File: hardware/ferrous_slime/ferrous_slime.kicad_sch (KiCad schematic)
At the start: 53 parts, among them J1 IMU_Connector, J2 Battery_Connector, J3 USB_C_Receptacle_USB2.0, J4 Unused_IO, Q1 DMG3415U, SW1 SW_PWR, U1 BNO/MPU/ICM_Break, U2 ESP32-C3-MINI-1, U3 TP4056, U4 M3406, Y1 32.768Hz

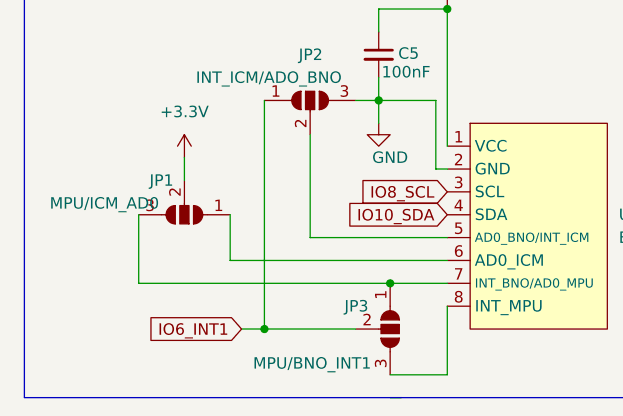
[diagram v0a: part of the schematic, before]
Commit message: Fixed jumper silkscreens and added double ground plane
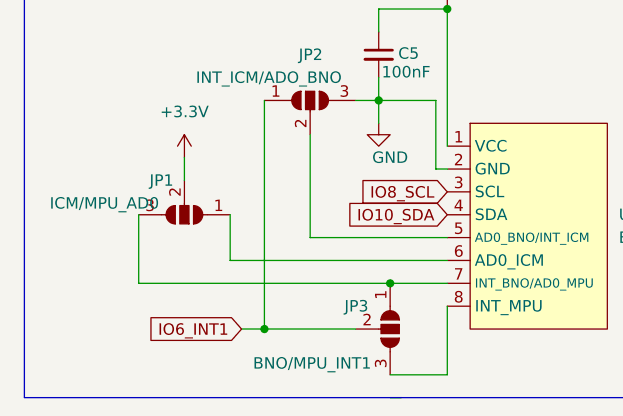
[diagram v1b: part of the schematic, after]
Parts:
- JP1: value MPU/ICM_AD0 -> ICM/MPU_AD0
- JP3: value MPU/BNO_INT1 -> BNO/MPU_INT1
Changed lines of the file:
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@@
       (effects (font (size 1.27 1.27)) (justify left))
     )
-    (property "Value" "MPU/BNO_INT1" (id 1) (at 39.37 161.29 90)
+    (property "Value" "BNO/MPU_INT1" (id 1) (at 39.37 161.29 90)
       (effects (font (size 1.27 1.27)) (justify left))
     )
@@
     (in_bom yes) (on_board yes)
     (property "Reference" "JP1" (id 0) (at 29.21 140.97 0))
-    (property "Value" "MPU/ICM_AD0" (id 1) (at 22.86 143.51 0))
+    (property "Value" "ICM/MPU_AD0" (id 1) (at 22.86 143.51 0))
     (property "Footprint" "Jumper:SolderJumper-3_P1.3mm_Open_Pad1.0x1.5mm" (id 2) (at 31.75 144.78 0)
       (effects (font (size 1.27 1.27)) hide)
@@
     )
     (path "/c4529189-45d4-4fb2-a639-86f5fb6b04c1"
-      (reference "JP1") (unit 1) (value "MPU/ICM_AD0") (footprint "Jumper:SolderJumper-3_P1.3mm_Open_Pad1.0x1.5mm")
+      (reference "JP1") (unit 1) (value "ICM/MPU_AD0") (footprint "Jumper:SolderJumper-3_P1.3mm_Open_Pad1.0x1.5mm")
     )
     (path "/3376fce4-7c2a-4830-8668-5c55f20711b2"
@@
     )
     (path "/9b1a0ddc-2815-4f35-824b-9e81fbeabbd5"
-      (reference "JP3") (unit 1) (value "MPU/BNO_INT1") (footprint "Jumper:SolderJumper-3_P1.3mm_Open_Pad1.0x1.5mm")
+      (reference "JP3") (unit 1) (value "BNO/MPU_INT1") (footprint "Jumper:SolderJumper-3_P1.3mm_Open_Pad1.0x1.5mm")
     )
     (path "/32aeb981-ffe8-4bff-a65d-ee3788161f8a"

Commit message: Annotated pins and added silkscreen art
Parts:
- J4: footprint Connector_PinHeader_2.54mm:PinHeader_1x07_P2.54mm_Vertical -> slimevr_pcb:IO_Breakouts
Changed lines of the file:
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@@
       (effects (font (size 1.27 1.27)) (justify left))
     )
-    (property "Footprint" "Connector_PinHeader_2.54mm:PinHeader_1x07_P2.54mm_Vertical" (id 2) (at 147.32 153.67 0)
+    (property "Footprint" "slimevr_pcb:IO_Breakouts" (id 2) (at 147.32 153.67 0)
       (effects (font (size 1.27 1.27)) hide)
     )
@@
     )
     (path "/07ba3b11-b85a-4d64-9bdc-e0f731b1e86f"
-      (reference "J4") (unit 1) (value "Unused_IO") (footprint "Connector_PinHeader_2.54mm:PinHeader_1x07_P2.54mm_Vertical")
+      (reference "J4") (unit 1) (value "Unused_IO") (footprint "slimevr_pcb:IO_Breakouts")
     )
     (path "/c4529189-45d4-4fb2-a639-86f5fb6b04c1"

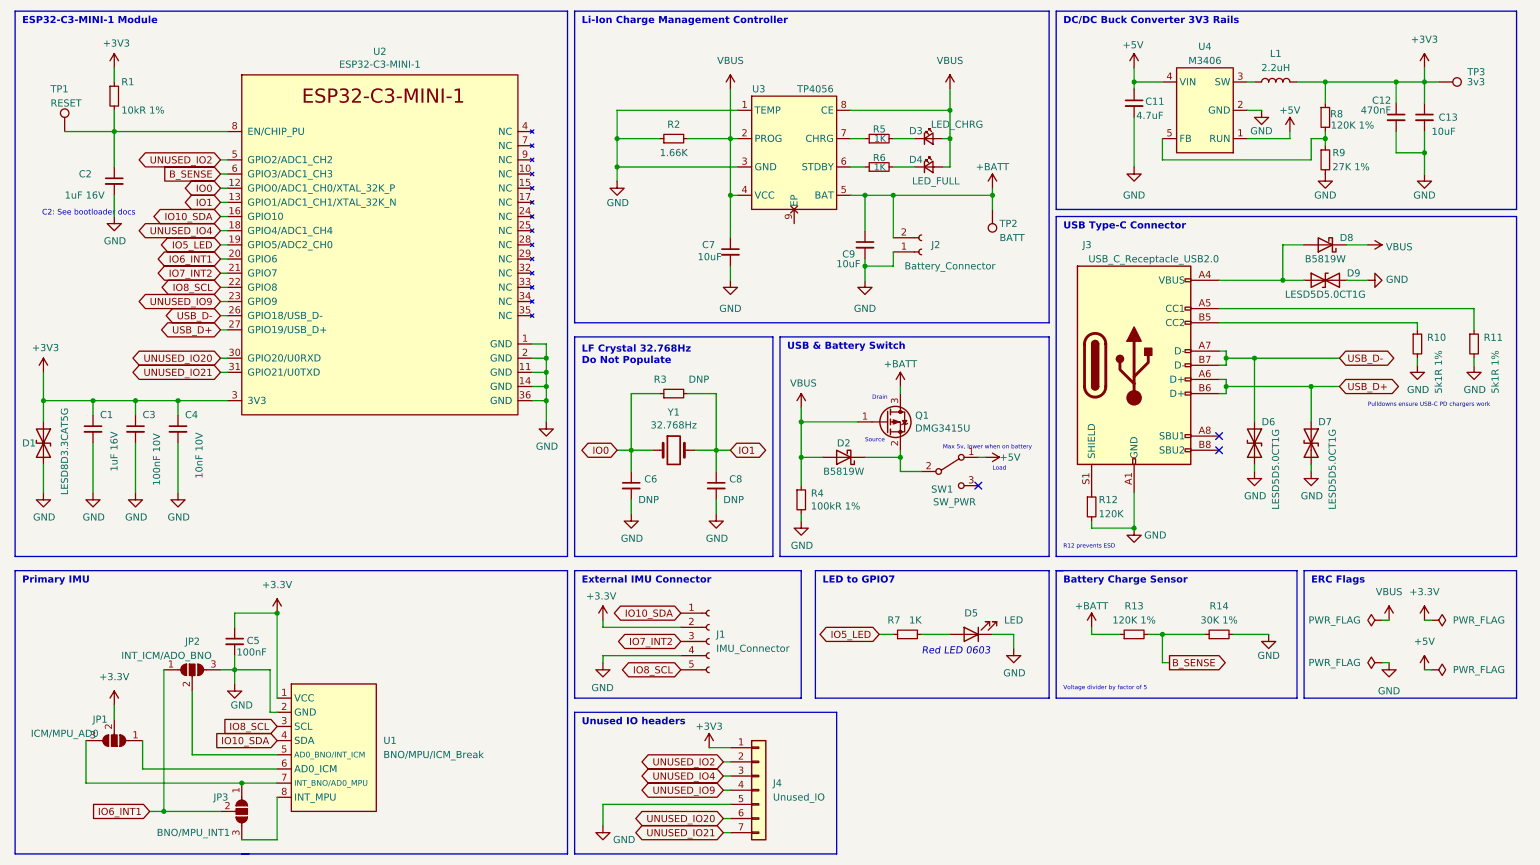
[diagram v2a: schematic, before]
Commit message: Removed Rust_Board and updated all renders/plots
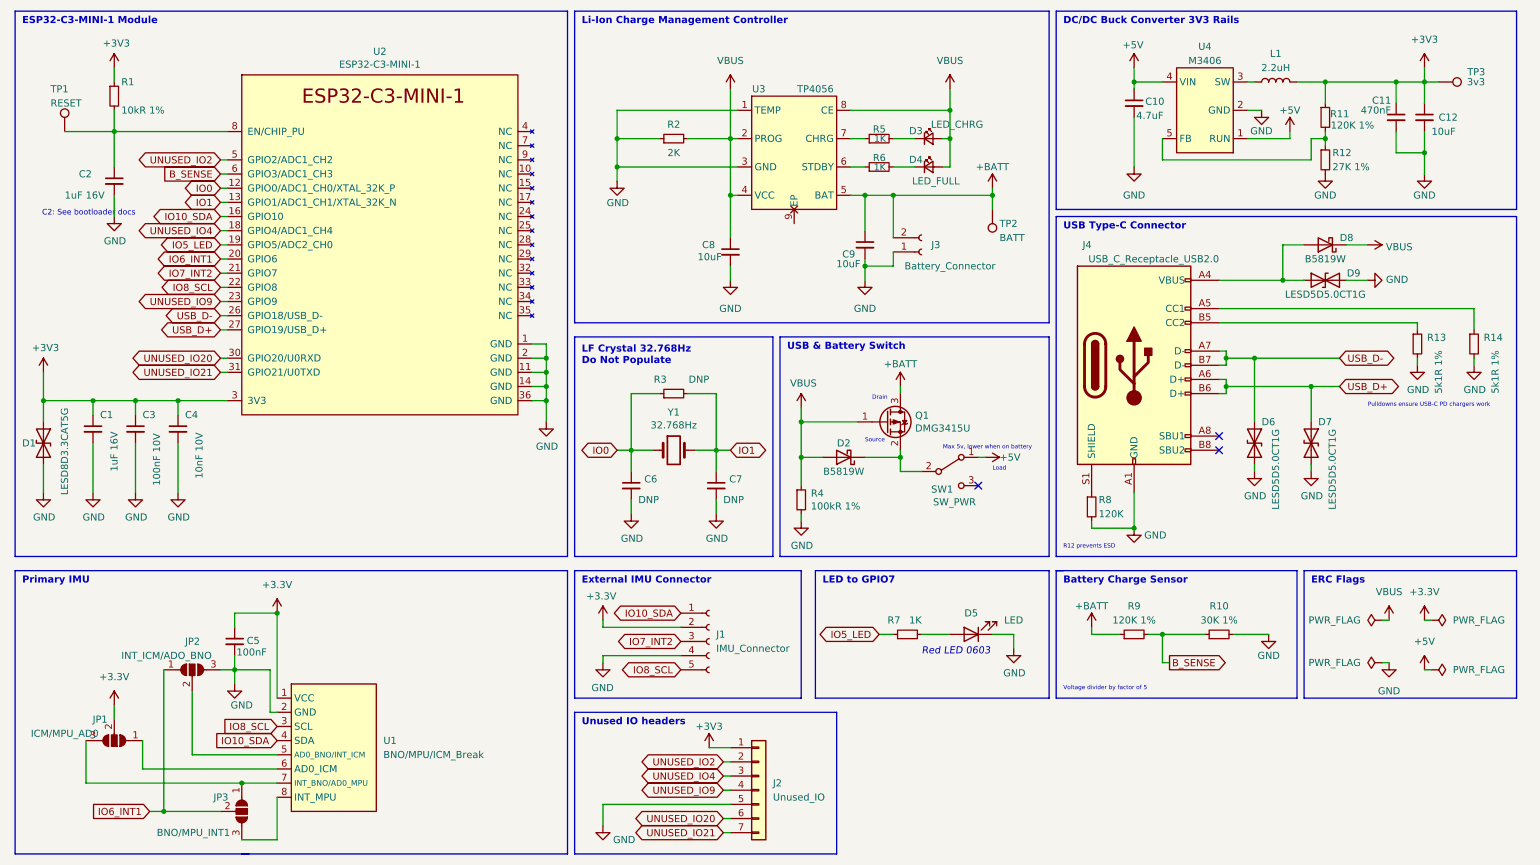
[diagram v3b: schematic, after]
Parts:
- R2: value 1.66K -> 2K
- renumbered C11 to C10, C12 to C11, C13 to C12, C8 to C7, C7 to C8, J4 to J2, J2 to J3, J3 to J4, R14 to R10, R8 to R11, R9 to R12, R10 to R13, R11 to R14, R12 to R8, R13 to R9

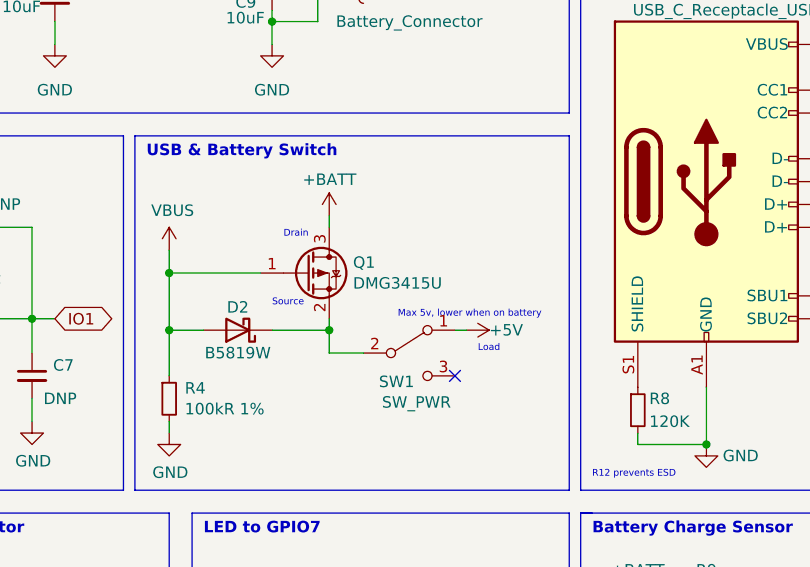
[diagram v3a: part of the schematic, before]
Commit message: Added refs to silkscreen
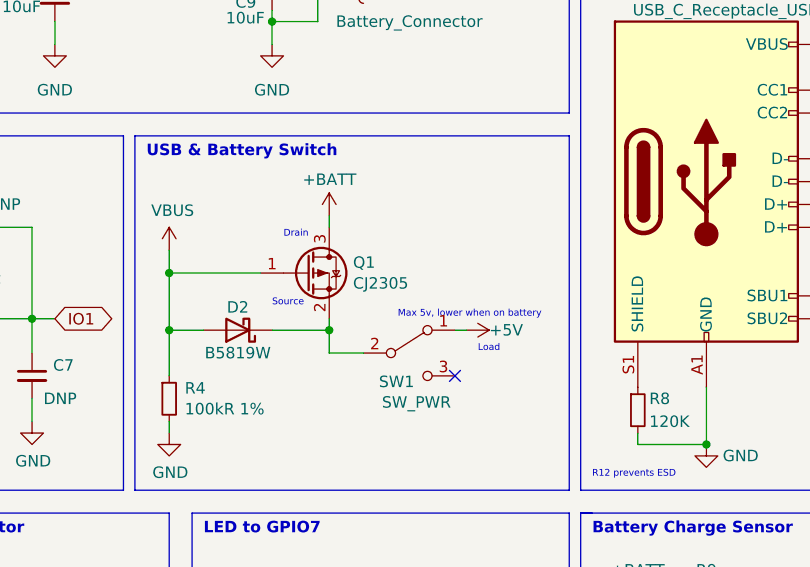
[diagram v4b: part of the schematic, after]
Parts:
- Q1: value DMG3415U -> CJ2305
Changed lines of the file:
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@@
       (effects (font (size 1.27 1.27)) (justify left))
     )
-    (property "Value" "DMG3415U" (id 1) (at 175.3616 88.773 0)
+    (property "Value" "CJ2305" (id 1) (at 175.3616 88.773 0)
       (effects (font (size 1.27 1.27)) (justify left))
     )
@@
     )
     (path "/00000000-0000-0000-0000-0000628bb66a"
-      (reference "Q1") (unit 1) (value "DMG3415U") (footprint "Package_TO_SOT_SMD:SOT-23")
+      (reference "Q1") (unit 1) (value "CJ2305") (footprint "Package_TO_SOT_SMD:SOT-23")
     )
     (path "/00000000-0000-0000-0000-000061cdb32a"

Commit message: v0.1.0 board released
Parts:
- D1: footprint Diode_SMD:D_SOD-323_HandSoldering -> slimevr_pcb:SOD882
- L1: footprint Inductor_SMD:L_7.3x7.3_H4.5 -> Inductor_SMD:L_Wuerth_MAPI-3015
- R4: value 100kR 1% -> 120K
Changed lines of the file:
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@@
   (symbol (lib_id "Device:D_TVS") (at 19.05 91.44 270) (unit 1)
     (in_bom yes) (on_board yes)
-    (property "Reference" "D1" (id 0) (at 15.24 91.44 90)
-      (effects (font (size 1.27 1.27)) (justify left))
-    )
-    (property "Value" "LESD8D3.3CAT5G" (id 1) (at 22.86 85.09 0)
-      (effects (font (size 1.27 1.27)) (justify left))
-    )
-    (property "Footprint" "Diode_SMD:D_SOD-323_HandSoldering" (id 2) (at 19.05 91.44 0)
+    (property "Reference" "D1" (id 0) (at 19.05 87.63 90)
+      (effects (font (size 1.27 1.27)) (justify left))
+    )
+    (property "Value" "LESD8D3.3CAT5G" (id 1) (at 16.51 83.82 0)
+      (effects (font (size 1.27 1.27)) (justify left))
+    )
+    (property "Footprint" "slimevr_pcb:SOD882" (id 2) (at 16.51 91.44 0)
       (effects (font (size 1.27 1.27)) hide)
     )
@@
       (effects (font (size 1.27 1.27)) (justify left))
     )
-    (property "Value" "100kR 1%" (id 1) (at 156.6672 102.743 0)
+    (property "Value" "120K" (id 1) (at 156.6672 102.743 0)
       (effects (font (size 1.27 1.27)) (justify left))
     )
@@
     (property "Reference" "L1" (id 0) (at 240.03 21.59 90))
     (property "Value" "2.2uH" (id 1) (at 240.03 24.13 90))
-    (property "Footprint" "Inductor_SMD:L_7.3x7.3_H4.5" (id 2) (at 240.03 26.67 0)
+    (property "Footprint" "Inductor_SMD:L_Wuerth_MAPI-3015" (id 2) (at 240.03 26.67 0)
       (effects (font (size 1.27 1.27)) hide)
     )
@@
     )
     (path "/00000000-0000-0000-0000-000062637b6c"
-      (reference "D1") (unit 1) (value "LESD8D3.3CAT5G") (footprint "Diode_SMD:D_SOD-323_HandSoldering")
+      (reference "D1") (unit 1) (value "LESD8D3.3CAT5G") (footprint "slimevr_pcb:SOD882")
     )
     (path "/00000000-0000-0000-0000-0000628c7e1d"
@@
     )
     (path "/32aeb981-ffe8-4bff-a65d-ee3788161f8a"
-      (reference "L1") (unit 1) (value "2.2uH") (footprint "Inductor_SMD:L_7.3x7.3_H4.5")
+      (reference "L1") (unit 1) (value "2.2uH") (footprint "Inductor_SMD:L_Wuerth_MAPI-3015")
     )
     (path "/00000000-0000-0000-0000-0000628bb66a"
@@
     )
     (path "/00000000-0000-0000-0000-0000628ca495"
-      (reference "R4") (unit 1) (value "100kR 1%") (footprint "Resistor_SMD:R_0603_1608Metric")
+      (reference "R4") (unit 1) (value "120K") (footprint "Resistor_SMD:R_0603_1608Metric")
     )
     (path "/1f6b4457-3275-408a-a5cc-c61e0857c7ff"
